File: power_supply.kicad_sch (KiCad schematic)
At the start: 24 parts, among them U3 ST1S10PHR, U4 ST1S09IPUR

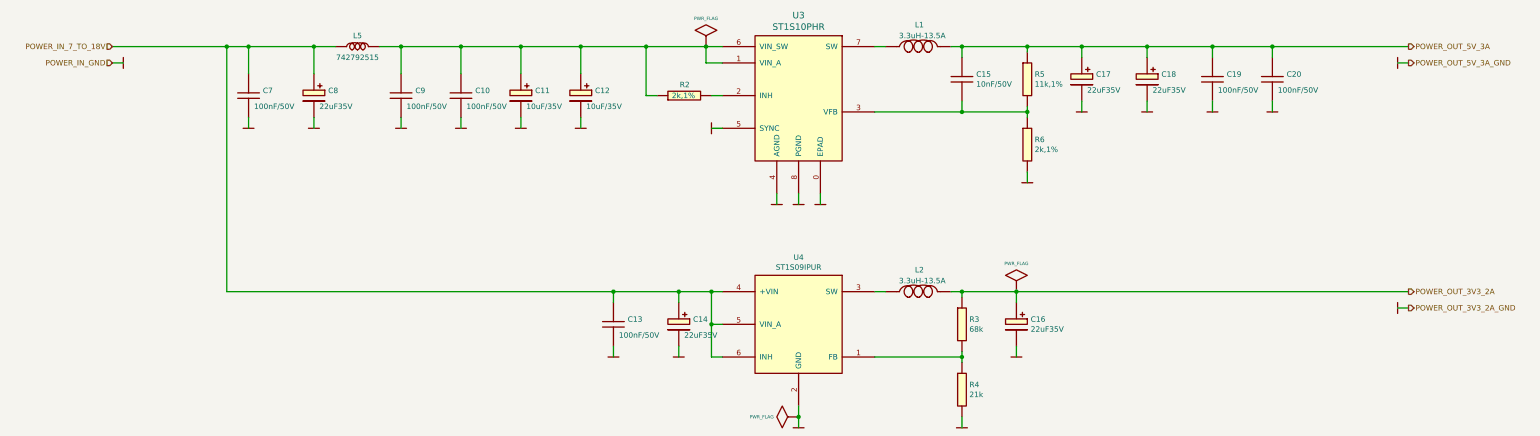
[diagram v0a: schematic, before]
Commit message: Changed supply of 3.3V DC-DC converter
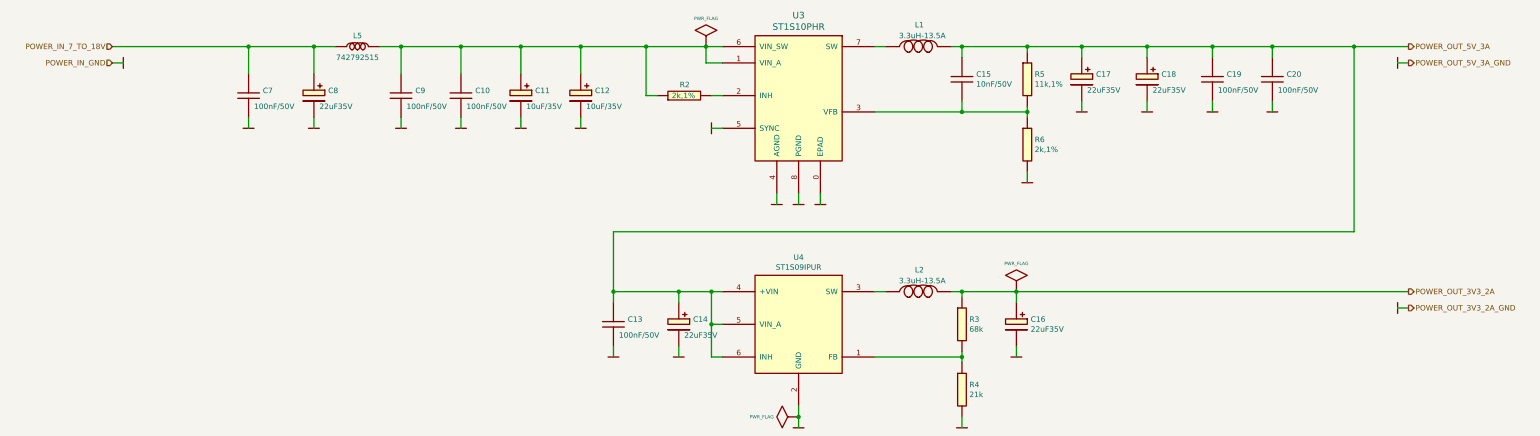
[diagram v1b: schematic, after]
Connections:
- net POWER_IN_7_TO_18V: no longer C13.1, C14.1, U4.4 (+VIN), U4.5 (VIN_A), U4.6 (INH)
- net POWER_OUT_5V_3A: now also C13.1, C14.1, U4.4 (+VIN), U4.5 (VIN_A), U4.6 (INH)
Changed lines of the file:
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@@
     (company "Embedded System Labs")
   )
-  (junction (at 80.01 102.87) (diameter 1.016) (color 0 0 0 0))
   (junction (at 85.09 102.87) (diameter 1.016) (color 0 0 0 0))
   (junction (at 100.33 102.87) (diameter 1.016) (color 0 0 0 0))
@@
   (junction (at 309.88 102.87) (diameter 1.016) (color 0 0 0 0))
   (junction (at 323.85 102.87) (diameter 1.016) (color 0 0 0 0))
-  (wire (pts (xy 53.34 102.87) (xy 80.01 102.87))
+  (junction (at 342.9 102.87) (diameter 1.016) (color 0 0 0 0))
+  (wire (pts (xy 53.34 102.87) (xy 85.09 102.87))
     (stroke (width 0) (type solid) (color 0 0 0 0))
   )
@@
     (stroke (width 0) (type solid) (color 0 0 0 0))
   )
-  (wire (pts (xy 80.01 102.87) (xy 80.01 160.02))
-    (stroke (width 0) (type solid) (color 0 0 0 0))
-  )
-  (wire (pts (xy 80.01 102.87) (xy 85.09 102.87))
-    (stroke (width 0) (type solid) (color 0 0 0 0))
-  )
   (wire (pts (xy 85.09 102.87) (xy 100.33 102.87))
     (stroke (width 0) (type solid) (color 0 0 0 0))
@@
     (stroke (width 0) (type solid) (color 0 0 0 0))
   )
-  (wire (pts (xy 170.18 160.02) (xy 80.01 160.02))
+  (wire (pts (xy 170.18 146.05) (xy 170.18 160.02))
     (stroke (width 0) (type solid) (color 0 0 0 0))
   )
@@
     (stroke (width 0) (type solid) (color 0 0 0 0))
   )
-  (wire (pts (xy 323.85 102.87) (xy 355.6 102.87))
+  (wire (pts (xy 323.85 102.87) (xy 342.9 102.87))
     (stroke (width 0) (type solid) (color 0 0 0 0))
   )
@@
     (stroke (width 0) (type solid) (color 0 0 0 0))
   )
+  (wire (pts (xy 342.9 102.87) (xy 342.9 146.05))
+    (stroke (width 0) (type solid) (color 0 0 0 0))
+  )
+  (wire (pts (xy 342.9 102.87) (xy 355.6 102.87))
+    (stroke (width 0) (type solid) (color 0 0 0 0))
+  )
+  (wire (pts (xy 342.9 146.05) (xy 170.18 146.05))
+    (stroke (width 0) (type solid) (color 0 0 0 0))
+  )

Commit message: Finalized project, regenerated gerbers
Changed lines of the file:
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@@
   (symbol (lib_id "Capacitors_Smd0603:100n") (at 170.18 167.64 0) (unit 1)
     (in_bom yes) (on_board yes)
-    (property "Reference" "C13" (id 0) (at 173.5074 166.4716 0)
+    (property "Reference" "C13" (id 0) (at 164.6174 165.2016 0)
       (effects (font (size 1.27 1.27)) (justify left))
     )
-    (property "Value" "100nF/50V" (id 1) (at 171.45 170.18 0)
+    (property "Value" "100nF/50V" (id 1) (at 158.75 170.18 0)
       (effects (font (size 1.27 1.27)) (justify left))
     )
@@
   (symbol (lib_id "Capacitors_Smd_Tantal:22uF_35V") (at 185.42 166.37 0) (unit 1)
     (in_bom yes) (on_board yes)
-    (property "Reference" "C14" (id 0) (at 188.7474 166.4716 0)
+    (property "Reference" "C14" (id 0) (at 179.8574 165.2016 0)
       (effects (font (size 1.27 1.27)) (justify left))
     )
-    (property "Value" "22uF35V" (id 1) (at 186.69 170.18 0)
+    (property "Value" "22uF35V" (id 1) (at 176.53 170.18 0)
       (effects (font (size 1.27 1.27)) (justify left))
     )
